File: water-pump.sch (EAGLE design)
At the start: 27 parts, among them U1 LDL1117S12R, U3 ATSAMD11C14A-SSUT

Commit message: minor adjustments to water pump
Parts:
- removed 1UF1: (no value), microbuilder:CAP_CERAMIC0603
- removed 1UF2, 1UF3: 10uF, microbuilder:CAP_CERAMIC0805
- removed D2: (no value), Adafruit:LEDCHIPLED_0805
- removed J3: (no value), SparkFun-Connectors:CONN_02PTH3
- removed J4: (no value), SparkFun-Connectors:CONN_04
- removed R3, R4: (no value), Adafruit:R-US_R0805
- added C4, C5: 10uF, microbuilder:CAP_CERAMIC0805
- added C6: 10uF, microbuilder:CAP_CERAMIC0603
- added D6: (no value), Adafruit:LEDCHIPLED_0805
- added F1: (no value), Adafruit:PTCFUSE-1812
- added J10: (no value), SparkFun-Connectors:CONN_02PTH3
- added R6: (no value), Adafruit:R-US_R0805
- D3: value (none) -> 3A/40V/500mV; device Adafruit:LEDCHIPLED_0805 -> SparkFun-DiscreteSemi:DIODE-SCHOTTKY-B340A
- J1: device EAGLE-INPUT_OUTPUT_CONNECTORS-rev17a:629105136821 -> SparkFun-Connectors:USB_MICRO-B_FEMALE-SMT
- J2: device SparkFun-Connectors:CONN_02PTH3 -> SparkFun-Connectors:CONN_05
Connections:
- net N$4 renamed USB+
- net N$5 renamed USB-
- net SIGNAL renamed BUS
- removed net 12V: 1UF3.P$2, D1.C, J2.1, U1.VIN
- new net 3.3V: C4.P$2, C6.P$1, J2.2, R6.2, U1.VOUT, U1.VOUT-1, U3.VDD
- new net RESET: J2.5, U3.PA28/!RST
- net GND: now also C4.P$1, C5.P$1, C6.P$2, J2.1; no longer 1UF1.P$2, 1UF2.P$1, 1UF3.P$1, D3.C, J4.1
- net N$1: now also J1.VBUS; no longer R3.1
- net N$6: now also D1.A, F1.1; no longer J1.VBUS, J3.2
- net N$7: now also D6.A, R6.1; no longer D2.A, R4.1
- net N$8: now also D6.C; no longer D2.C
- net PUMP: now also J10.2; no longer J2.2
- net SWCLK: now also J2.4; no longer J4.4
- net SWDIO: now also J2.3; no longer J4.3
- net VCC: now also C5.P$2, D1.C, D3.C, J10.1, U1.VIN; no longer 1UF1.P$1, 1UF2.P$2, J4.2, R3.2, R4.2, U1.VOUT, U1.VOUT-1, U3.VDD
- net VCC-RAW: now also F1.2; no longer D1.A, J3.1
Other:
- moved on the sheet: D1, Q1, R1, R2, U1, U3

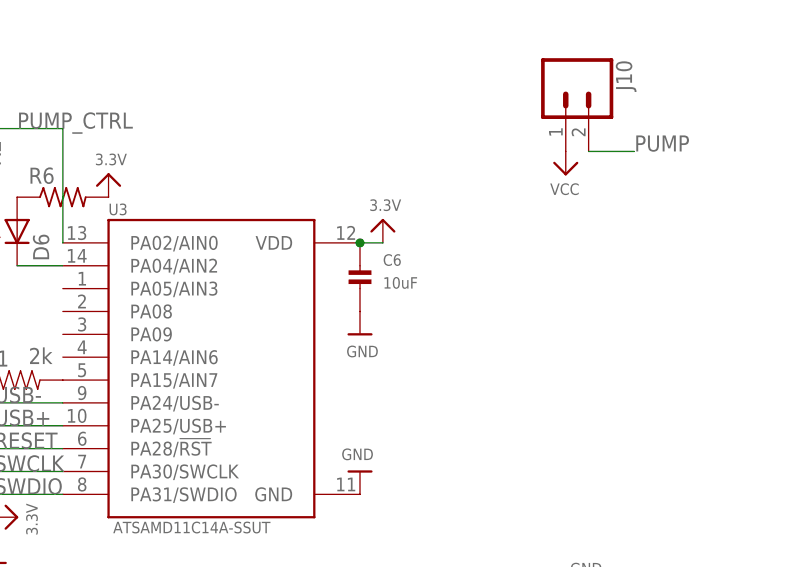
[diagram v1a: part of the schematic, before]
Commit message: modified c6 to 1uF
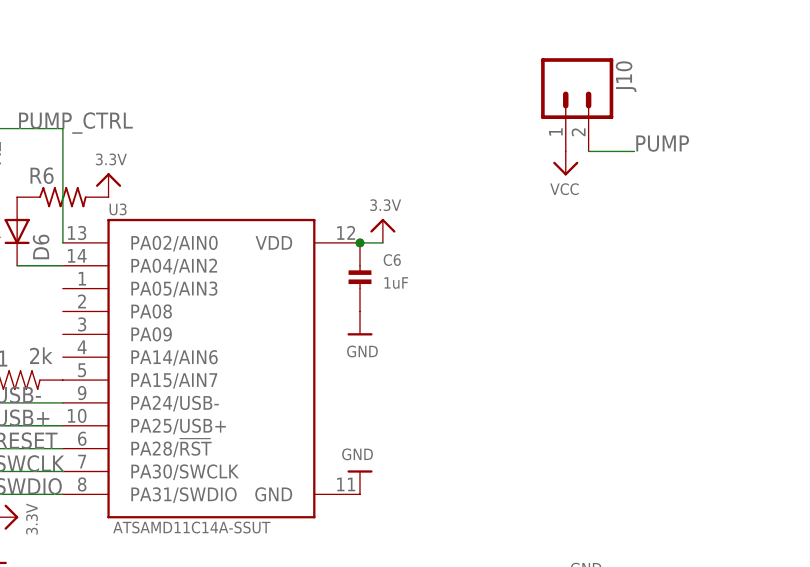
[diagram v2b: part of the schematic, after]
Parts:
- C6: value 10uF -> 1uF
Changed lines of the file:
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@@
 <part name="FRAME1" library="frames" library_urn="urn:adsk.eagle:library:229" deviceset="A4L-LOC" device=""/>
 <part name="P+4" library="microbuilder" deviceset="VCC" device=""/>
-<part name="C6" library="microbuilder" deviceset="CAP_CERAMIC" device="0603" value="10uF"/>
+<part name="C6" library="microbuilder" deviceset="CAP_CERAMIC" device="0603" value="1uF"/>
 <part name="U$3" library="microbuilder" deviceset="GND" device=""/>
 <part name="U1" library="LDL1117S12R" deviceset="LDL1117S12R" device=""/>
